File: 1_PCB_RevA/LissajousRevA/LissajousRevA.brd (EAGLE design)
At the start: 100 x 80 mm, 87 parts, among them U101 LM348D, U201 LM348D, U401 LM348D

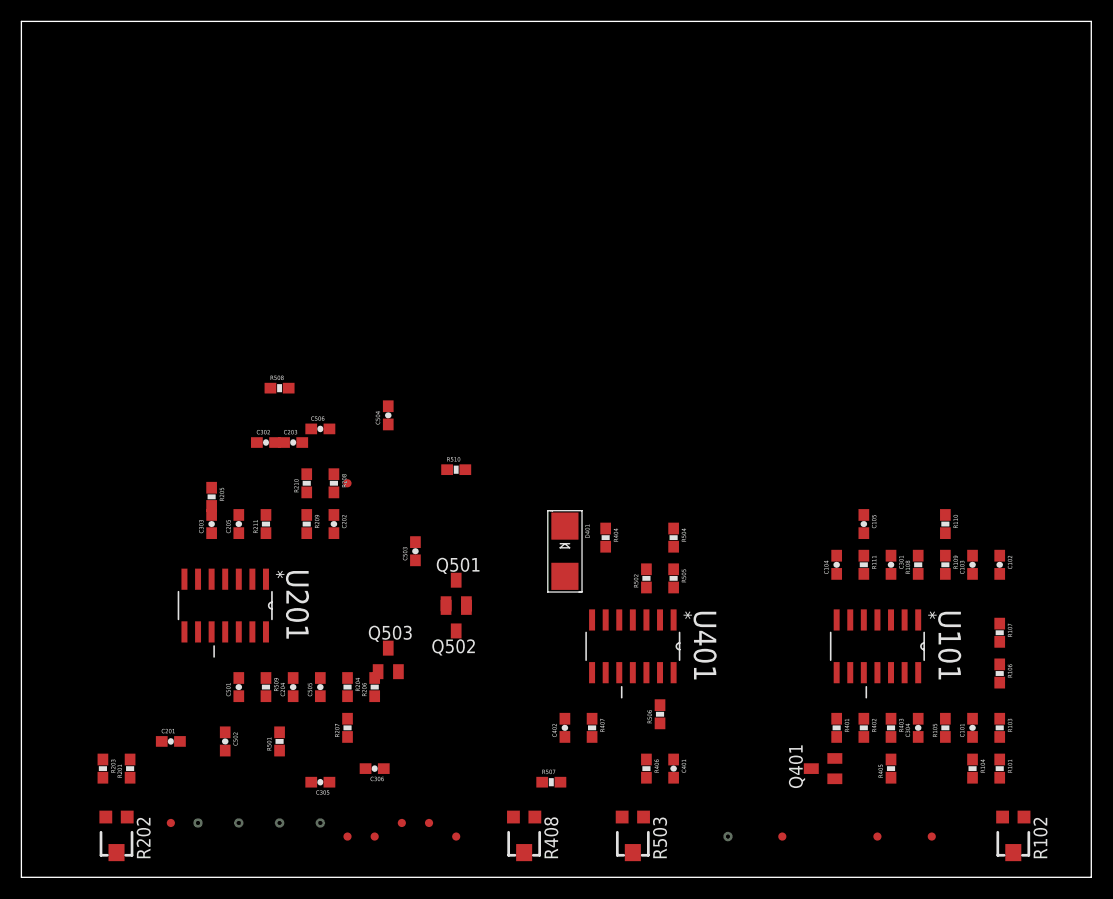
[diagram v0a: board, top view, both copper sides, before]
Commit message: sch net fix and more placement
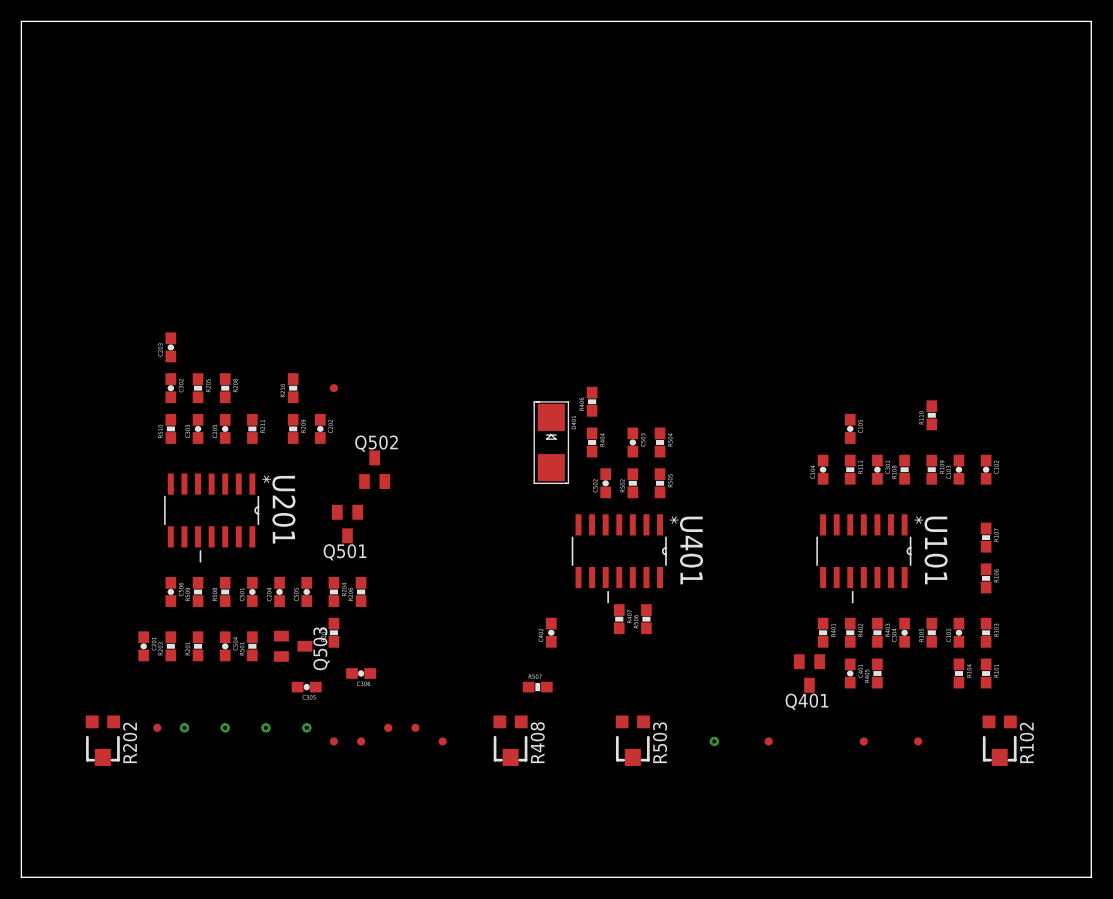
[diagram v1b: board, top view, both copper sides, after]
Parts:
- moved C502 43.0 mm to (54.6, 36.8), turned to 90 degrees
- moved R406 34.7 mm to (53.3, 44.5), turned to 90 degrees
- moved R510 26.9 mm to (14.0, 41.9), turned to 90 degrees
- moved C504 26.4 mm to (19.1, 21.6), turned to 270 degrees
- moved C503 22.7 mm to (57.1, 40.6), turned to 270 degrees
- moved C506 20.7 mm to (14.0, 26.7), turned to 270 degrees
- moved R508 19.7 mm to (19.1, 26.7), turned to 90 degrees
- moved C401 18.8 mm to (77.5, 19.1)
- moved Q502 15.9 mm to (33.0, 38.1), turned to 0 degrees
- moved C203 14.5 mm to (14.0, 49.5), turned to 90 degrees
- moved R208 13.5 mm to (19.1, 45.7)
- moved R201 13.1 mm to (16.5, 21.6)
- moved R203 13.1 mm to (14.0, 21.6), turned to 90 degrees
- moved Q501 12.0 mm to (30.5, 33.0), turned to 180 degrees
- moved R509 10.9 mm to (16.5, 26.7), turned to 90 degrees
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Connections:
- removed net N$35: C506.2
- net N$46: now also C506.1
- net VIEW2: now also C506.2; no longer C506.1

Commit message: lots of routing and another net fix
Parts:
- moved TP305 36.9 mm to (2.54, 41.9)
- moved TP501 35.3 mm to (52.1, 44.5)
- moved R501 31.4 mm to (33.0, 50.8)
- moved TP401 28.7 mm to (67.3, 19.1)
- moved TP301 25.3 mm to (15.2, 38.1)
- moved C204 24.4 mm to (27.9, 50.8), turned to 270 degrees
- moved TP202 24.1 mm to (24.1, 35.6)
- moved C303 22.9 mm to (39.4, 40.6), turned to 270 degrees
- moved D401 20.5 mm to (39.4, 58.4), turned to 180 degrees
- moved C506 20.1 mm to (7.62, 45.7), turned to 90 degrees
- moved Q401 19.0 mm to (54.6, 19.1), turned to 270 degrees
- moved Q503 17.7 mm to (31.8, 38.1), turned to 0 degrees
- moved C501 16.6 mm to (12.7, 40.6), turned to 270 degrees
- moved R402 16.6 mm to (61.0, 21.6)
- moved TP502 16.6 mm to (43.2, 21.6)
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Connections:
- removed net N$41: C504.2
- net N$39: now also C504.2
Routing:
- net 0V: track 0.00 -> 259.7 mm, vias 0 -> 10
- net N$39: track 0.00 -> 65.5 mm, vias 0 -> 2
- net N$2: track 0.00 -> 56.0 mm
- net N$7: track 0.00 -> 52.5 mm
- net N$20: track 0.00 -> 51.0 mm, vias 0 -> 3
- net SINEGEN2: track 0.00 -> 36.9 mm, vias 0 -> 2
- net N$24: track 0.00 -> 34.5 mm
- net N$9: track 0.00 -> 33.9 mm
- net VIEW1: track 0.00 -> 32.3 mm, vias 0 -> 2
- net N$26: track 0.00 -> 31.1 mm
- net N$46: track 0.00 -> 28.2 mm
- net N$12: track 0.00 -> 28.1 mm
- net N$31: track 0.00 -> 28.0 mm, vias 0 -> 2
- net N$45: track 0.00 -> 27.3 mm, vias 0 -> 2
- net N$37: track 0.00 -> 26.9 mm
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
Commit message: removed test points, can just use legs instead
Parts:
- removed TP101, TP102, TP103, TP201, TP202, TP203, TP401, TP402, TP501, TP502: TEST-POINT3, passives:PAD.03X.03
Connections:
- net N$15: no longer TP201.P$1
- net N$21: no longer TP202.P$1
- net N$29: no longer TP501.P$1
- net N$30: no longer TP401.P$1
- net N$32: no longer TP402.P$1
- net N$42: no longer TP502.P$1
- net N$7: no longer TP101.P$1
- net N$8: no longer TP102.P$1
- net SINEGEN1: no longer TP103.P$1
- net SINEGEN2: no longer TP203.P$1
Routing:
- net N$42: track 10.1 -> 8.88 mm
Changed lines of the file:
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@@
 <element name="R106" library="passives" package="0603-RES" value="0R" x="86.36" y="29.21" rot="R270"/>
 <element name="R109" library="passives" package="0603-RES" value="0R" x="81.28" y="40.64" rot="R270"/>
-<element name="TP101" library="passives" package="PAD.03X.03" value="TEST-POINT3" x="76.2" y="12.7"/>
-<element name="TP102" library="passives" package="PAD.03X.03" value="TEST-POINT3" x="74.93" y="12.7"/>
-<element name="TP103" library="passives" package="PAD.03X.03" value="TEST-POINT3" x="73.66" y="12.7"/>
 <element name="U201" library="LM348D" package="SOIC127P600X175-14N" value="LM348D" x="17.78" y="33.02" rot="R270">
 <attribute name="PACKAGE" value="SOIC-14" x="8.89" y="-1.27" size="1.778" layer="27" rot="R270" display="off"/>
@@
 <element name="R206" library="passives" package="0603-RES" value="0R" x="31.75" y="25.4" rot="R90"/>
 <element name="R209" library="passives" package="0603-RES" value="0R" x="22.86" y="40.64" rot="R270"/>
-<element name="TP201" library="passives" package="PAD.03X.03" value="TEST-POINT3" x="12.7" y="13.97"/>
-<element name="TP202" library="passives" package="PAD.03X.03" value="TEST-POINT3" x="24.13" y="35.56"/>
-<element name="TP203" library="passives" package="PAD.03X.03" value="TEST-POINT3" x="25.4" y="54.61"/>
 <element name="TP301" library="passives" package="TP_15TH" value="TEST-POINTTP_15TH_THRU" x="15.24" y="38.1"/>
 <element name="TP303" library="passives" package="TP_15TH" value="TEST-POINTTP_15TH_THRU" x="17.78" y="21.59"/>
@@
 <element name="R402" library="passives" package="0603-RES" value="0R" x="60.96" y="21.59" rot="R270"/>
 <element name="R403" library="passives" package="0603-RES" value="DNF" x="76.2" y="21.59" rot="R90"/>
-<element name="TP401" library="passives" package="PAD.03X.03" value="TEST-POINT3" x="67.31" y="19.05"/>
-<element name="TP402" library="passives" package="PAD.03X.03" value="TEST-POINT3" x="36.83" y="13.97"/>
 <element name="Q501" library="adafruit" package="SOT23" value="" x="31.75" y="30.48"/>
 <element name="C501" library="passives" package="0603-CAP" value="10nF" x="12.7" y="40.64" rot="R270"/>
@@
 <element name="R509" library="passives" package="0603-RES" value="33K" x="7.62" y="25.4" rot="R90"/>
 <element name="R510" library="passives" package="0603-RES" value="33K" x="7.62" y="50.8" rot="R270"/>
-<element name="TP501" library="passives" package="PAD.03X.03" value="TEST-POINT3" x="52.07" y="44.45"/>
-<element name="TP502" library="passives" package="PAD.03X.03" value="TEST-POINT3" x="43.18" y="21.59"/>
 <element name="TP305" library="passives" package="TP_15TH" value="TEST-POINTTP_15TH_THRU" x="2.54" y="41.91"/>
 <element name="TP304" library="passives" package="TP_15TH" value="TEST-POINTTP_15TH_THRU" x="72.39" y="12.7"/>
@@
 <contactref element="R101" pad="1"/>
 <contactref element="R102" pad="1"/>
-<contactref element="TP101" pad="P$1"/>
 <wire x1="86.36" y1="28.36" x2="83.4" y2="28.36" width="0.4064" layer="1"/>
 <wire x1="83.4" y1="28.36" x2="81.28" y2="30.48" width="0.4064" layer="1"/>
@@
 <wire x1="87.63" y1="7.62" x2="88.9" y2="8.89" width="0.4064" layer="1"/>
 <wire x1="88.9" y1="8.89" x2="88.9" y2="27.94" width="0.4064" layer="1"/>
-<wire x1="76.2" y1="12.7" x2="84.09" y2="10.875" width="0" layer="19" extent="1-1"/>
 </signal>
 <signal name="N$5">
@@
 <contactref element="U101" pad="2"/>
 <contactref element="R109" pad="2"/>
-<contactref element="TP102" pad="P$1"/>
 <wire x1="73.66" y1="35.4838" x2="74.93" y2="35.4838" width="0.4064" layer="1"/>
 <wire x1="81.28" y1="39.79" x2="79.16" y2="39.79" width="0.4064" layer="1"/>
@@
 <wire x1="81.28" y1="39.79" x2="82.97" y2="39.79" width="0.4064" layer="1"/>
 <wire x1="82.97" y1="39.79" x2="84.67" y2="41.49" width="0.4064" layer="1"/>
-<wire x1="74.93" y1="12.7" x2="74.93" y2="35.4838" width="0" layer="19" extent="1-1"/>
 </signal>
 <signal name="N$3">
@@
 <contactref element="R201" pad="1"/>
 <contactref element="R202" pad="1"/>
-<contactref element="TP201" pad="P$1"/>
 <wire x1="22.86" y1="26.25" x2="22.86" y2="29.2862" width="0.4064" layer="1"/>
 <wire x1="22.86" y1="29.2862" x2="21.59" y2="30.5562" width="0.4064" layer="1"/>
@@
 <wire x1="26.5938" y1="30.5562" x2="27.94" y2="29.21" width="0.4064" layer="1"/>
 <wire x1="27.94" y1="26.25" x2="27.94" y2="29.21" width="0.4064" layer="1"/>
-<wire x1="12.7" y1="13.97" x2="22.86" y2="26.25" width="0" layer="19" extent="1-1"/>
-<wire x1="8.62" y1="14.525" x2="12.7" y2="13.97" width="0" layer="19" extent="1-1"/>
 <wire x1="27.94" y1="26.25" x2="31.75" y2="26.25" width="0.4064" layer="1"/>
+<wire x1="8.62" y1="14.525" x2="22.86" y2="26.25" width="0" layer="19" extent="1-1"/>
 </signal>
 <signal name="N$16">
@@
 <contactref element="U201" pad="6"/>
 <contactref element="U201" pad="7"/>
-<contactref element="TP203" pad="P$1"/>
 <contactref element="C501" pad="2"/>
 <contactref element="R501" pad="1"/>
@@
 <via x="12.7" y="35.56" extent="1-16" drill="0.6"/>
 <wire x1="12.7" y1="35.56" x2="12.7" y2="36.83" width="0.4064" layer="1"/>
-<wire x1="27.94" y1="49.95" x2="25.4" y2="54.61" width="0" layer="19" extent="1-1"/>
 </signal>
 <signal name="N$21">
@@
 <contactref element="U201" pad="2"/>
 <contactref element="R209" pad="2"/>
-<contactref element="TP202" pad="P$1"/>
 <wire x1="22.86" y1="39.79" x2="22.86" y2="36.7538" width="0.4064" layer="1"/>
 <wire x1="22.86" y1="36.7538" x2="21.59" y2="35.4838" width="0.4064" layer="1"/>
@@
 <wire x1="27.94" y1="39.79" x2="22.86" y2="39.79" width="0.4064" layer="1"/>
 <wire x1="21.59" y1="35.4838" x2="24.0538" y2="35.4838" width="0.4064" layer="1"/>
-<wire x1="24.0538" y1="35.4838" x2="24.13" y2="35.56" width="0.4064" layer="1"/>
 </signal>
 <signal name="N$22">
@@
 <contactref element="U101" pad="6"/>
 <contactref element="U101" pad="7"/>
-<contactref element="TP103" pad="P$1"/>
 <wire x1="66.04" y1="39.79" x2="66.04" y2="36.7538" width="0.4064" layer="1"/>
 <wire x1="66.04" y1="36.7538" x2="67.31" y2="35.4838" width="0.4064" layer="1"/>
@@
 <wire x1="68.58" y1="33.02" x2="68.58" y2="35.4838" width="0.4064" layer="1"/>
 <wire x1="67.31" y1="35.4838" x2="68.58" y2="35.4838" width="0.4064" layer="1"/>
-<wire x1="73.66" y1="12.7" x2="69.85" y2="30.5562" width="0" layer="19" extent="1-1"/>
 </signal>
 <signal name="N$27">
@@
 <contactref element="C402" pad="1"/>
 <contactref element="Q401" pad="1"/>
-<contactref element="TP402" pad="P$1"/>
 <wire x1="39.37" y1="30.5562" x2="39.37" y2="30.48" width="0.4064" layer="1"/>
 <wire x1="39.37" y1="30.48" x2="38.1" y2="29.21" width="0.4064" layer="1"/>
@@
 <wire x1="40.64" y1="24.55" x2="53.51" y2="20" width="0" layer="19" extent="1-1"/>
 <wire x1="35.56" y1="26.25" x2="38.1" y2="25.4" width="0" layer="19" extent="1-1"/>
-<wire x1="36.83" y1="13.97" x2="38.95" y2="24.55" width="0" layer="19" extent="1-1"/>
 </signal>
 <signal name="N$30">
@@
 <contactref element="C401" pad="2"/>
 <contactref element="R405" pad="1"/>
-<contactref element="TP401" pad="P$1"/>
 <wire x1="66.04" y1="20.74" x2="71.12" y2="20.74" width="0.4064" layer="1"/>
 <wire x1="39.37" y1="49.95" x2="39.37" y2="46.57" width="0.4064" layer="1"/>
 <wire x1="39.37" y1="49.95" x2="41.7195" y2="58.42" width="0" layer="19" extent="1-1"/>
-<wire x1="67.31" y1="19.05" x2="39.37" y2="46.57" width="0" layer="19" extent="1-1"/>
-<wire x1="66.04" y1="20.74" x2="67.31" y2="19.05" width="0" layer="19" extent="1-1"/>
+<wire x1="66.04" y1="20.74" x2="39.37" y2="46.57" width="0" layer="19" extent="1-1"/>
 </signal>
 <signal name="N$34">
@@
 <contactref element="C503" pad="2"/>
 <contactref element="R505" pad="1"/>
-<contactref element="TP501" pad="P$1"/>
 <wire x1="54.61" y1="41.49" x2="54.61" y2="43.6" width="0.4064" layer="1"/>
 <wire x1="49.53" y1="41.49" x2="49.53" y2="43.18" width="0.4064" layer="1"/>
@@
 <wire x1="44.87" y1="44.45" x2="44.45" y2="44.87" width="0.4064" layer="1"/>
 <wire x1="49.53" y1="41.49" x2="54.61" y2="41.49" width="0.4064" layer="1"/>
-<wire x1="52.07" y1="44.45" x2="49.53" y2="41.49" width="0" layer="19" extent="1-1"/>
 </signal>
 <signal name="N$36">
@@
 <contactref element="C505" pad="2"/>
 <contactref element="R508" pad="1"/>
-<contactref element="TP502" pad="P$1"/>
 <wire x1="12.7" y1="21.17" x2="12.7" y2="24.55" width="0.4064" layer="1"/>
 <wire x1="40.64" y1="22.44" x2="42.33" y2="22.44" width="0.4064" layer="1"/>
-<wire x1="42.33" y1="22.44" x2="43.18" y2="21.59" width="0.4064" layer="1"/>
+<wire x1="12.7" y1="21.17" x2="8.89" y2="21.17" width="0.4064" layer="1"/>
 <wire x1="12.7" y1="21.17" x2="40.64" y2="22.44" width="0" layer="19" extent="1-1"/>
-<wire x1="12.7" y1="21.17" x2="8.89" y2="21.17" width="0.4064" layer="1"/>
 </signal>
 <signal name="N$45">

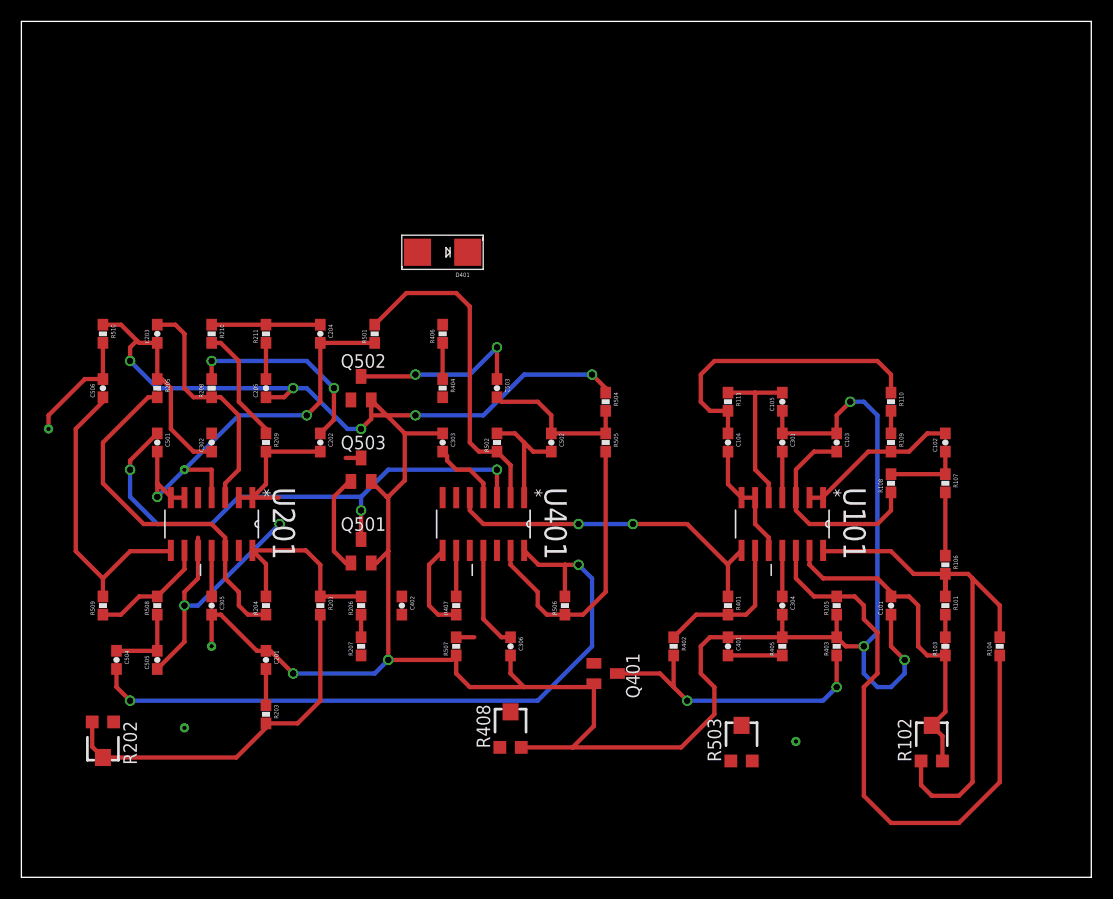
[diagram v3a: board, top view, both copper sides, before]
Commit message: nearly fully routed, lots tp optimise though
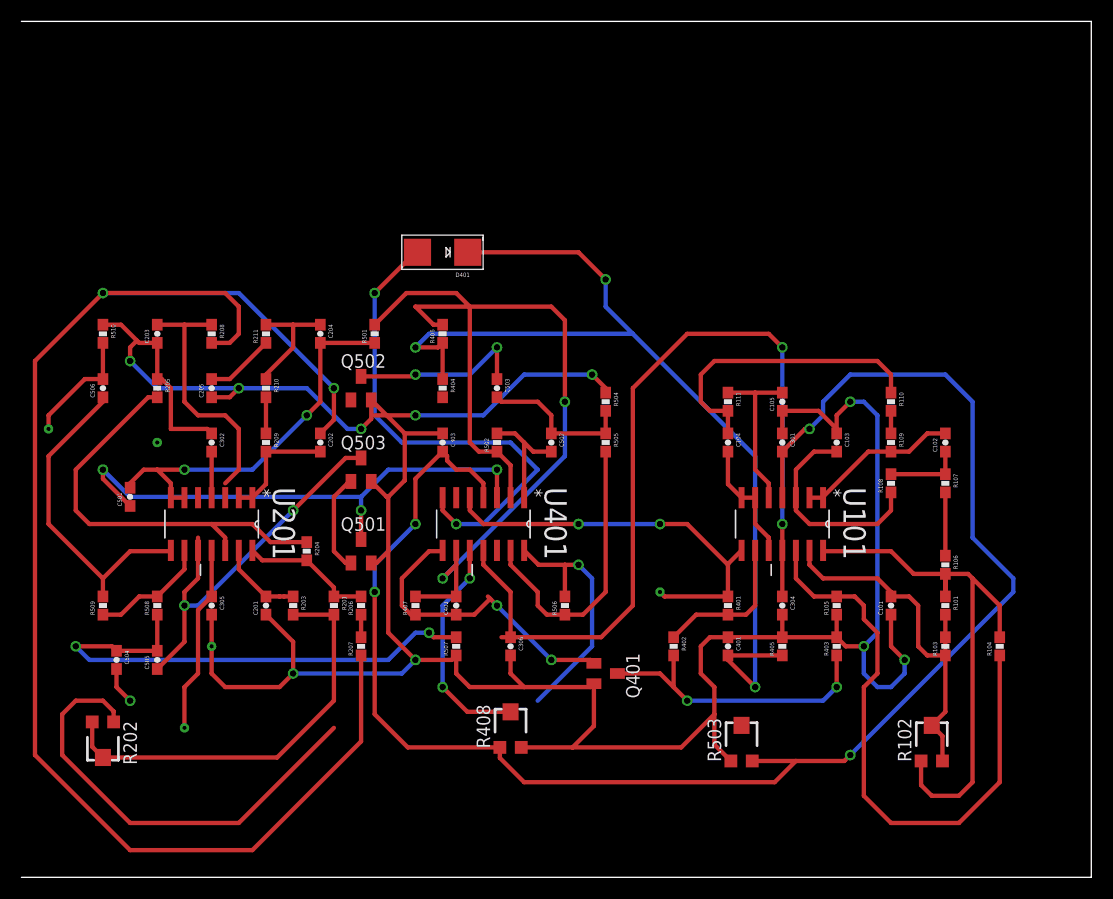
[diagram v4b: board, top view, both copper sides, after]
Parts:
- moved TP304 18.9 mm to (59.7, 26.7)
- moved R203 10.5 mm to (25.4, 25.4)
- moved R210 7.18 mm to (22.9, 45.7)
- moved R204 6.35 mm to (26.7, 30.5), turned to 270 degrees
- moved C501 5.68 mm to (10.2, 35.6), turned to 90 degrees
- moved C201 5.08 mm to (22.9, 25.4), turned to 90 degrees
- moved C205 5.08 mm to (17.8, 45.7)
- moved C402 5.08 mm to (40.6, 25.4), turned to 90 degrees
- moved R208 5.08 mm to (17.8, 50.8), turned to 270 degrees
- moved R407 3.81 mm to (36.8, 25.4)
- moved TP301 3.59 mm to (12.7, 40.6), turned to 90 degrees
- moved R201 1.27 mm to (29.2, 25.4)
- turned C302 to 270 degrees
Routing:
- net V+: track 16.1 -> 158.7 mm, vias 0 -> 4
- net N$17: track 18.9 -> 140.9 mm
- net N$30: track 8.46 -> 93.9 mm, vias 0 -> 3
- net V-: track 18.3 -> 100.5 mm, vias 0 -> 2
- net N$25: track 4.31 -> 56.5 mm, vias 0 -> 2
- net N$28: track 0.00 -> 47.1 mm, vias 0 -> 2
- net N$42: track 8.88 -> 48.5 mm, vias 0 -> 2
- net N$39: track 65.5 -> 27.4 mm
- net N$15: track 18.5 -> 54.7 mm
- net N$34: track 0.00 -> 21.1 mm, vias 0 -> 2
- net N$32: track 8.57 -> 29.2 mm, vias 0 -> 2
- net 0V: track 259.7 -> 274.1 mm
- net N$45: track 27.3 -> 36.1 mm
- net N$23: track 11.1 -> 3.38 mm
- net VIEW1: track 32.3 -> 38.8 mm
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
